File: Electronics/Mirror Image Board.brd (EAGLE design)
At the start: 61.5 x 47 mm, 19 parts, among them IC2 7805L

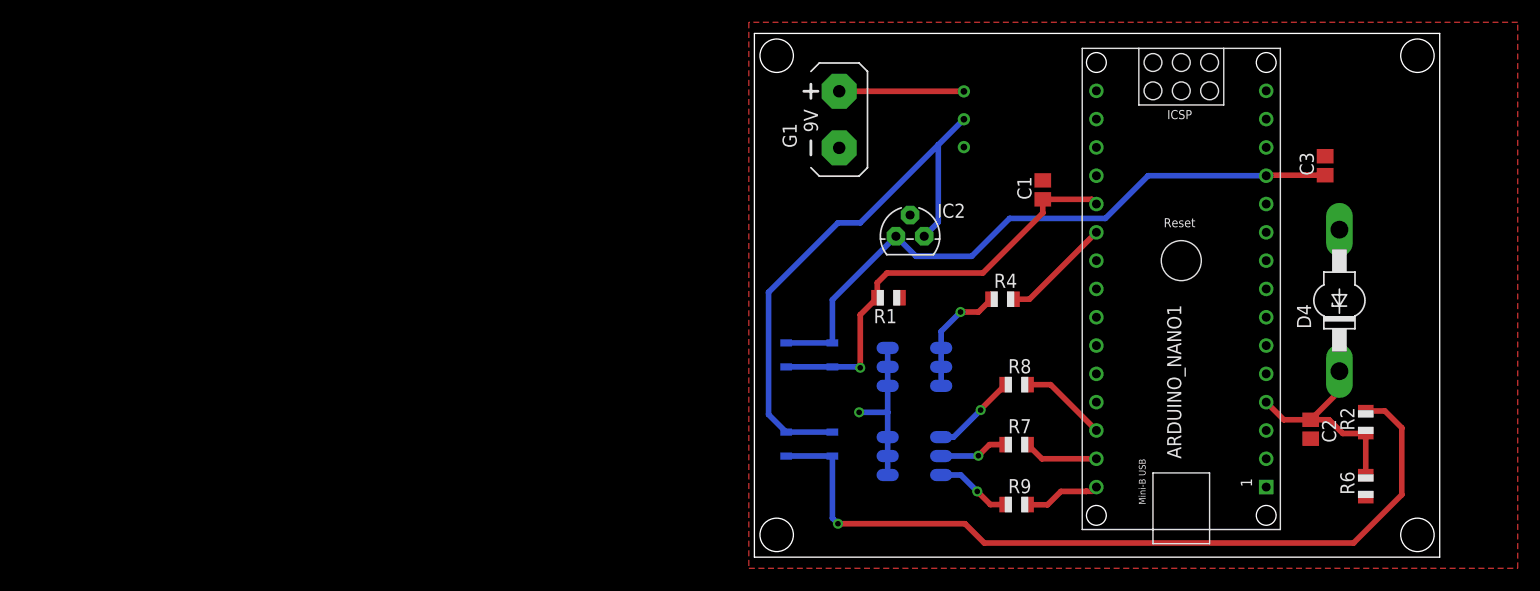
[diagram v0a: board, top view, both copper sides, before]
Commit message: Changing resistor values and uploading mirror image of board
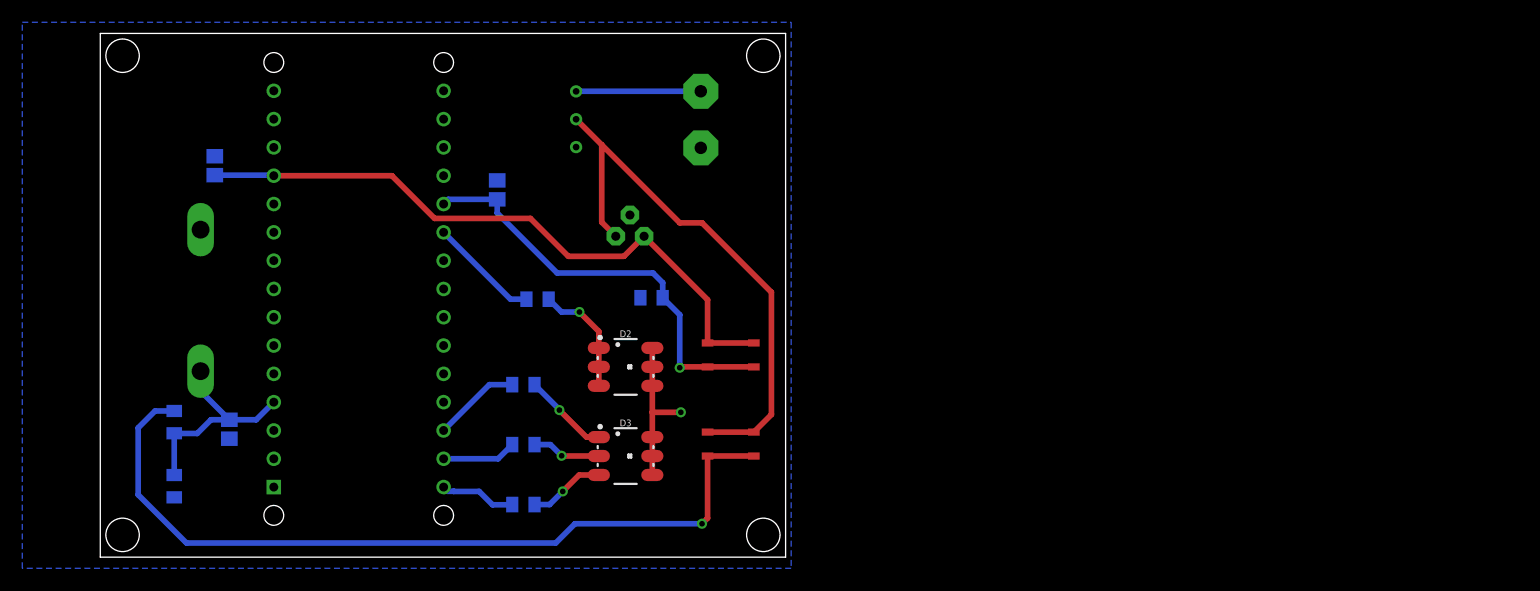
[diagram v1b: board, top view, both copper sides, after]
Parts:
- moved R2 106.9 mm to (-52.1, 12.1), flipped to the bottom
- moved R6 106.9 mm to (-52.1, 6.37), flipped to the bottom
- moved D4 102.2 mm to (-49.7, 23.0), flipped to the bottom
- moved C3 99.6 mm to (-48.4, 35.1), flipped to the bottom
- moved C2 97.0 mm to (-47.1, 11.5), flipped to the bottom
- moved ARDUINO_NANO1 73.8 mm to (-35.5, 26.6), flipped to the bottom
- moved C1 49.0 mm to (-23.1, 33.0), flipped to the bottom
- moved R7 44.3 mm to (-20.7, 10.1), flipped to the bottom
- moved R8 44.3 mm to (-20.7, 15.5), flipped to the bottom
- moved R9 44.3 mm to (-20.7, 4.72), flipped to the bottom
- moved R4 41.7 mm to (-19.5, 23.1), flipped to the bottom
- moved U$3 34.8 mm to (-16.0, 41.8), flipped to the bottom
- moved D2 25.9 mm to (-11.6, 17.1), flipped to the top
- moved D3 25.9 mm to (-11.6, 9.07), flipped to the top
- moved IC2 25.1 mm to (-11.2, 28.8), flipped to the bottom
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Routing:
- added copper zone on layer 16, net GND
- removed copper zone on layer 1, net GND
